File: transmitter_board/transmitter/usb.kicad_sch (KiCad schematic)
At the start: 3 parts

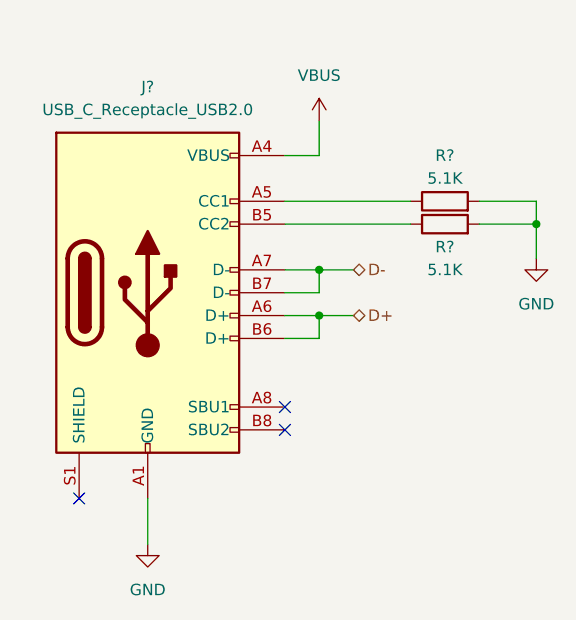
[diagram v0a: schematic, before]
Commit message: finished board schematic
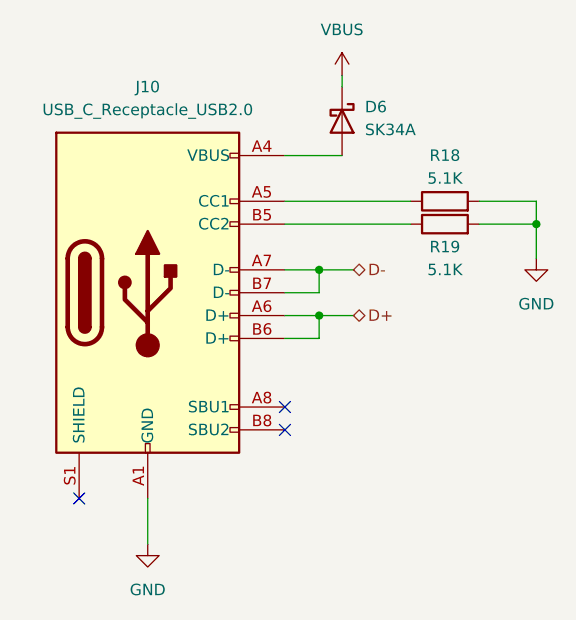
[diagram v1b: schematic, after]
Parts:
- added D6: SK34A, Diode_SMD:D_SMA, symbol Diode:B150-E3
- gave numbers to parts that had none: 3
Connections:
- net VBUS: now also D6.1 (K); no longer J10.A4 (VBUS), J10.A9 (VBUS), J10.B4 (VBUS), J10.B9 (VBUS)
- new net: D6.2 (A), J10.A4 (VBUS), J10.A9 (VBUS), J10.B4 (VBUS), J10.B9 (VBUS)
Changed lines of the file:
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@@
-    (stroke (width 0) (type default) (color 0 0 0 0))
-  )
-  (wire (pts (xy 156.21 88.9) (xy 152.4 88.9))
     (stroke (width 0) (type default) (color 0 0 0 0))
   )
@@
     (stroke (width 0) (type default) (color 0 0 0 0))
   )
-  (wire (pts (xy 152.4 109.22) (xy 156.21 109.22))
+  (wire (pts (xy 152.4 88.9) (xy 158.75 88.9))
     (stroke (width 0) (type default) (color 0 0 0 0))
   )
-  (wire (pts (xy 156.21 85.09) (xy 156.21 88.9))
+  (wire (pts (xy 158.75 80.01) (xy 158.75 81.28))
+    (stroke (width 0) (type default) (color 0 0 0 0))
+  )
+  (wire (pts (xy 152.4 109.22) (xy 156.21 109.22))
     (stroke (width 0) (type default) (color 0 0 0 0))
   )
@@
     (effects (font (size 1.27 1.27)) (justify left))
   )
-  (symbol (lib_id "power:VBUS") (at 156.21 85.09 0) (unit 1)
+  (symbol (lib_id "power:VBUS") (at 158.75 80.01 0) (unit 1)
     (in_bom yes) (on_board yes) (fields_autoplaced)
-    (property "Reference" "#PWR?" (id 0) (at 156.21 88.9 0)
+    (property "Reference" "#PWR0137" (id 0) (at 158.75 83.82 0)
       (effects (font (size 1.27 1.27)) hide)
     )
-    (property "Value" "VBUS" (id 1) (at 156.21 80.01 0))
-    (property "Footprint" "" (id 2) (at 156.21 85.09 0)
+    (property "Value" "VBUS" (id 1) (at 158.75 74.93 0))
+    (property "Footprint" "" (id 2) (at 158.75 80.01 0)
       (effects (font (size 1.27 1.27)) hide)
     )
-    (property "Datasheet" "" (id 3) (at 156.21 85.09 0)
+    (property "Datasheet" "" (id 3) (at 158.75 80.01 0)
       (effects (font (size 1.27 1.27)) hide)
     )
     (pin "1")
   )
+  (symbol (lib_id "Diode:B150-E3") (at 158.75 85.09 270) (unit 1)
+    (in_bom yes) (on_board yes) (fields_autoplaced)
+    (property "Reference" "D6" (id 0) (at 161.29 83.5024 90)
+      (effects (font (size 1.27 1.27)) (justify left))
+    )
+    (property "Value" "SK34A" (id 1) (at 161.29 86.0424 90)
+      (effects (font (size 1.27 1.27)) (justify left))
+    )
+    (property "Footprint" "Diode_SMD:D_SMA" (id 2) (at 154.305 85.09 0)
+      (effects (font (size 1.27 1.27)) hide)
+    )
+    (property "Datasheet" "http://www.vishay.com/docs/88946/b120.pdf" (id 3) (at 158.75 85.09 0)
+      (effects (font (size 1.27 1.27)) hide)
+    )
+    (pin "1")
+    (pin "2")
+  )
   (symbol (lib_id "power:GND") (at 180.34 100.33 0) (unit 1)
     (in_bom yes) (on_board yes) (fields_autoplaced)
-    (property "Reference" "#PWR?" (id 0) (at 180.34 106.68 0)
+    (property "Reference" "#PWR0136" (id 0) (at 180.34 106.68 0)
       (effects (font (size 1.27 1.27)) hide)
     )
@@
   (symbol (lib_id "Connector:USB_C_Receptacle_USB2.0") (at 137.16 104.14 0) (unit 1)
     (in_bom yes) (on_board yes) (fields_autoplaced)
-    (property "Reference" "J?" (id 0) (at 137.16 81.28 0))
+    (property "Reference" "J10" (id 0) (at 137.16 81.28 0))
     (property "Value" "USB_C_Receptacle_USB2.0" (id 1) (at 137.16 83.82 0))
     (property "Footprint" "" (id 2) (at 140.97 104.14 0)
@@
   (symbol (lib_id "Device:R") (at 170.18 96.52 90) (unit 1)
     (in_bom yes) (on_board yes)
-    (property "Reference" "R?" (id 0) (at 170.18 99.06 90))
+    (property "Reference" "R19" (id 0) (at 170.18 99.06 90))
     (property "Value" "5.1K" (id 1) (at 170.18 101.6 90))
     (property "Footprint" "" (id 2) (at 170.18 98.298 90)
@@
   (symbol (lib_id "Device:R") (at 170.18 93.98 90) (unit 1)
     (in_bom yes) (on_board yes)
-    (property "Reference" "R?" (id 0) (at 170.18 88.9 90))
+    (property "Reference" "R18" (id 0) (at 170.18 88.9 90))
     (property "Value" "5.1K" (id 1) (at 170.18 91.44 90))
     (property "Footprint" "" (id 2) (at 170.18 95.758 90)
@@
   (symbol (lib_id "power:GND") (at 137.16 132.08 0) (unit 1)
     (in_bom yes) (on_board yes) (fields_autoplaced)
-    (property "Reference" "#PWR?" (id 0) (at 137.16 138.43 0)
+    (property "Reference" "#PWR0135" (id 0) (at 137.16 138.43 0)
       (effects (font (size 1.27 1.27)) hide)
     )
